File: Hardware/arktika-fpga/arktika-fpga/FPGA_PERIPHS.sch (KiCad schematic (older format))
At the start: 29 parts

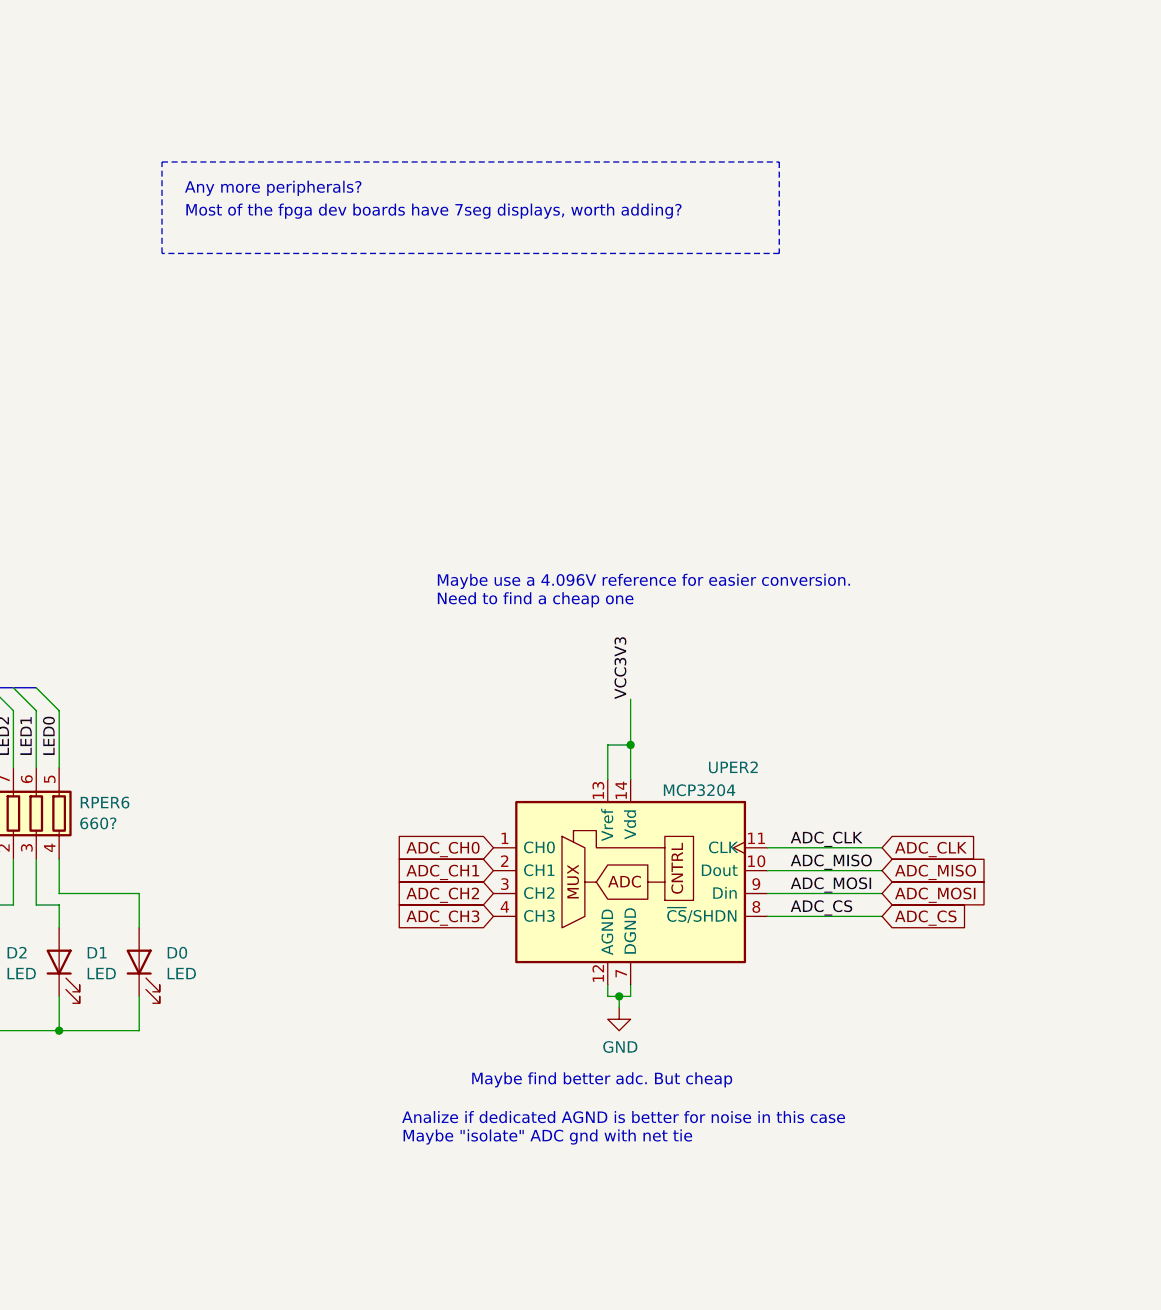
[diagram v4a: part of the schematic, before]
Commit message: Finished routing, did gnd planes, added more silkscreen and some manual via stitching. Pre-final layout.
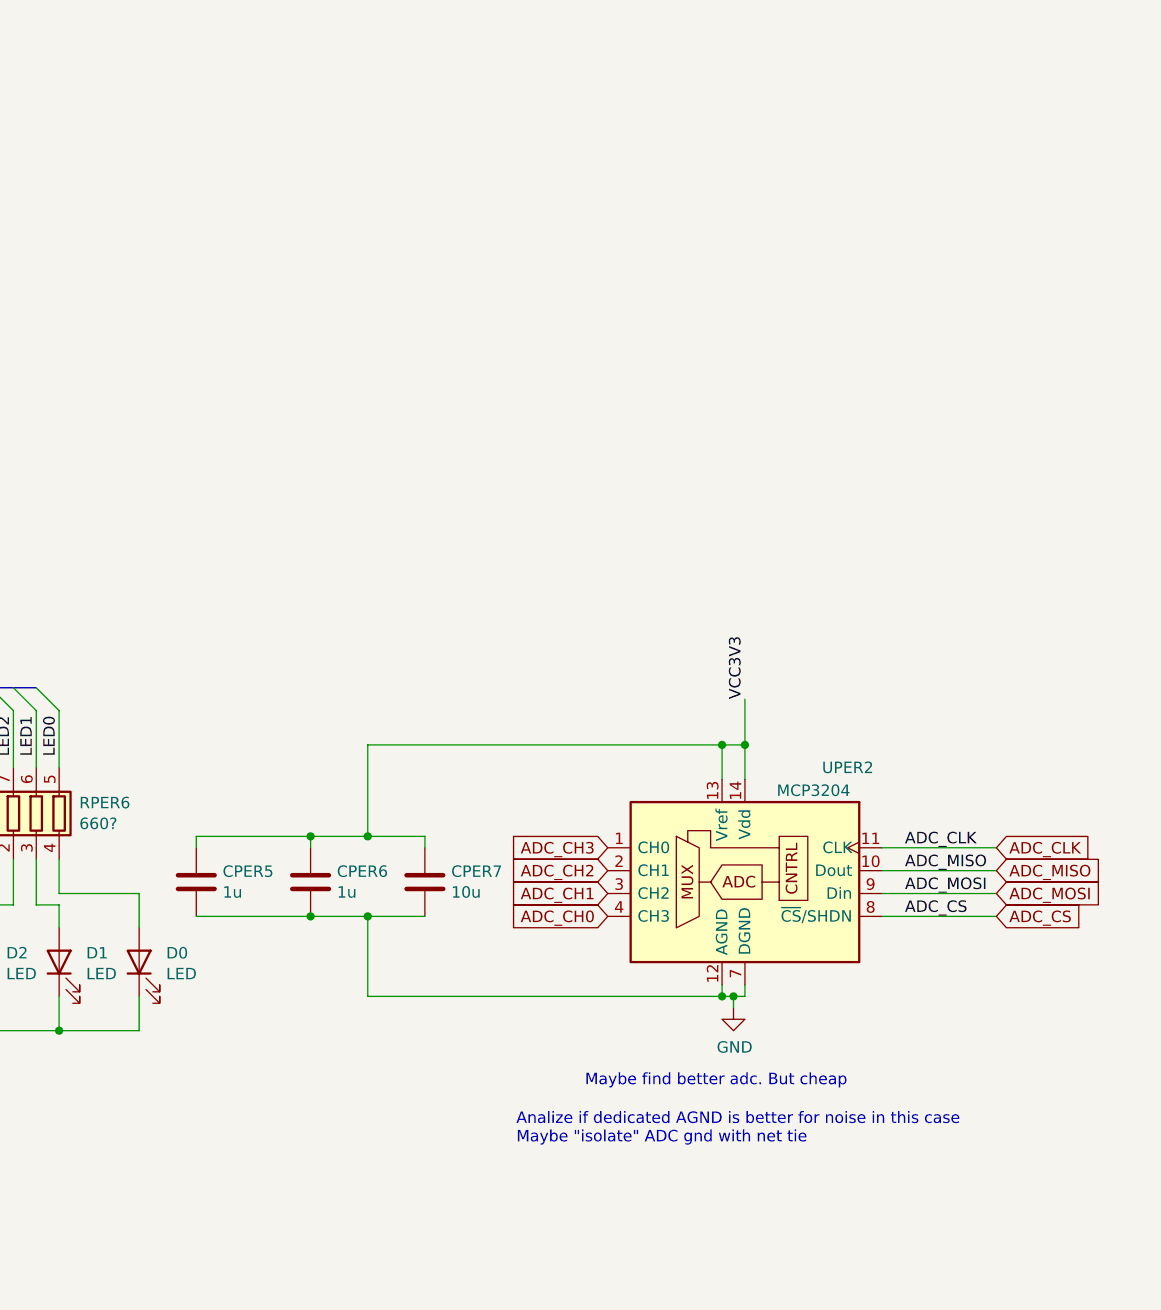
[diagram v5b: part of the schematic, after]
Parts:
- added CPER5, CPER6: 1u, Capacitor_SMD:C_0603_1608Metric_Pad1.05x0.95mm_HandSolder, symbol arktika-fpga-rescue:C-Device
- added CPER7: 10u, Capacitor_SMD:C_0603_1608Metric_Pad1.05x0.95mm_HandSolder, symbol arktika-fpga-rescue:C-Device
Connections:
- net ADC_CH0: now also UPER2.4 (CH3); no longer UPER2.1 (CH0)
- net ADC_CH1: now also UPER2.3 (CH2); no longer UPER2.2 (CH1)
- net ADC_CH2: now also UPER2.2 (CH1); no longer UPER2.3 (CH2)
- net ADC_CH3: now also UPER2.1 (CH0); no longer UPER2.4 (CH3)
- net GND: now also CPER5.2, CPER6.2, CPER7.2
- net VCC3V3: now also CPER5.1, CPER6.1, CPER7.1
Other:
- note removed: "Any more peripherals?"
- note removed: "Maybe use a 4.096V reference for easier conversion.\nNeed to find a cheap one"
- note removed: "Most of the fpga dev boards have 7seg displays, worth adding?"
- moved on the sheet: UPER2
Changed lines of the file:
@@
 L arktika-fpga-rescue:MCP3204-Analog_ADC UPER2
 U 1 1 5F72040D
-P 8950 5000
+P 9450 5000
 AR Path="/5F72040D" Ref="UPER2"  Part="1"
 AR Path="/5F72015E/5F72040D" Ref="UPER2"  Part="1"
-F 0 "UPER2" H 9400 5450 50  0000 C CNN
-F 1 "MCP3204" H 9250 5350 50  0000 C CNN
-F 2 "Package_SO:SOIC-14_3.9x8.7mm_P1.27mm" H 9850 4700 50  0001 C CNN
-F 3 "http://ww1.microchip.com/downloads/en/DeviceDoc/21298c.pdf" H 9850 4700 50  0001 C CNN
-	1    8950 5000
+F 0 "UPER2" H 9900 5450 50  0000 C CNN
+F 1 "MCP3204" H 9750 5350 50  0000 C CNN
+F 2 "Package_SO:SOIC-14_3.9x8.7mm_P1.27mm" H 10350 4700 50  0001 C CNN
+F 3 "http://ww1.microchip.com/downloads/en/DeviceDoc/21298c.pdf" H 10350 4700 50  0001 C CNN
+	1    9450 5000
 	1    0    0    -1
 $EndComp
@@
 	1    0    0    -1
 $EndComp
-Text Label 9650 4900 0    50   ~ 0
+Text Label 10150 4900 0    50   ~ 0
 ADC_CLK
-Text Label 9650 5000 0    50   ~ 0
+Text Label 10150 5000 0    50   ~ 0
 ADC_MISO
-Text Label 9650 5100 0    50   ~ 0
+Text Label 10150 5100 0    50   ~ 0
 ADC_MOSI
-Text Label 9650 5200 0    50   ~ 0
+Text Label 10150 5200 0    50   ~ 0
 ADC_CS
 Wire Wire Line
-	9550 4900 10050 4900
-Wire Wire Line
-	10050 5000 9550 5000
-Wire Wire Line
-	9550 5100 10050 5100
-Wire Wire Line
-	10050 5200 9550 5200
+	10050 4900 10550 4900
+Wire Wire Line
+	10550 5000 10050 5000
+Wire Wire Line
+	10050 5100 10550 5100
+Wire Wire Line
+	10550 5200 10050 5200
 Text HLabel 1250 7200 0    50   Input ~ 0
 SW[0..7]
@@
 Text Label 1800 950  0    50   ~ 0
 VCC3V3
-Text Notes 8250 5950 0    50   ~ 0
+Text Notes 8750 5950 0    50   ~ 0
 Maybe find better adc. But cheap\n
 Text Notes 2850 800  0    50   ~ 0
@@
 L arktika-fpga-rescue:GND-power #PWR0155
 U 1 1 5F6F2DE0
-P 8900 5600
-F 0 "#PWR0155" H 8900 5350 50  0001 C CNN
-F 1 "GND" H 8905 5427 50  0000 C CNN
-F 2 "" H 8900 5600 50  0001 C CNN
-F 3 "" H 8900 5600 50  0001 C CNN
-	1    8900 5600
-	1    0    0    -1
-$EndComp
-Wire Wire Line
-	8850 5500 8850 5550
-Wire Wire Line
-	8850 5550 8900 5550
-Wire Wire Line
-	8950 5550 8950 5500
-Wire Wire Line
-	8900 5550 8900 5600
-Connection ~ 8900 5550
-Wire Wire Line
-	8900 5550 8950 5550
-Text Notes 7950 6200 0    50   ~ 0
+P 9400 5600
+F 0 "#PWR0155" H 9400 5350 50  0001 C CNN
+F 1 "GND" H 9405 5427 50  0000 C CNN
+F 2 "" H 9400 5600 50  0001 C CNN
+F 3 "" H 9400 5600 50  0001 C CNN
+	1    9400 5600
+	1    0    0    -1
+$EndComp
+Wire Wire Line
+	9350 5500 9350 5550
+Wire Wire Line
+	9350 5550 9400 5550
+Wire Wire Line
+	9450 5550 9450 5500
+Wire Wire Line
+	9400 5550 9400 5600
+Connection ~ 9400 5550
+Wire Wire Line
+	9400 5550 9450 5550
+Text Notes 8450 6200 0    50   ~ 0
 Analize if dedicated AGND is better for noise in this case\nMaybe "isolate" ADC gnd with net tie
-Text Label 8950 4250 1    50   ~ 0
+Text Label 9450 4250 1    50   ~ 0
 VCC3V3
 Wire Wire Line
-	8950 4250 8950 4450
-Wire Wire Line
-	8850 4600 8850 4450
-Wire Wire Line
-	8850 4450 8950 4450
-Connection ~ 8950 4450
-Wire Wire Line
-	8950 4450 8950 4600
-Text Notes 8100 3850 0    50   ~ 0
-Maybe use a 4.096V reference for easier conversion.\nNeed to find a cheap one
-Text Notes 7000 2050 0    50   ~ 0
-Any more peripherals?
-Text Notes 7000 2150 0    50   ~ 0
-Most of the fpga dev boards have 7seg displays, worth adding?
-Wire Notes Line
-	6900 1900 9600 1900
-Wire Notes Line
-	9600 1900 9600 2300
-Wire Notes Line
-	9600 2300 6900 2300
-Wire Notes Line
-	6900 2300 6900 1900
+	9450 4250 9450 4450
+Wire Wire Line
+	9350 4600 9350 4450
+Wire Wire Line
+	9350 4450 9450 4450
+Connection ~ 9450 4450
+Wire Wire Line
+	9450 4450 9450 4600
 Connection ~ 2250 1600
 Wire Wire Line
@@
 Text Label 1350 7300 0    50   ~ 0
 LED[0..7]
-Text GLabel 8350 4900 0    50   Input ~ 0
+Text GLabel 8850 5200 0    50   Input ~ 0
 ADC_CH0
-Text GLabel 8350 5000 0    50   Input ~ 0
+Text GLabel 8850 5100 0    50   Input ~ 0
 ADC_CH1
-Text GLabel 8350 5100 0    50   Input ~ 0
+Text GLabel 8850 5000 0    50   Input ~ 0
 ADC_CH2
-Text GLabel 8350 5200 0    50   Input ~ 0
+Text GLabel 8850 4900 0    50   Input ~ 0
 ADC_CH3
-Text GLabel 10050 4900 2    50   Input ~ 0
+Text GLabel 10550 4900 2    50   Input ~ 0
 ADC_CLK
-Text GLabel 10050 5000 2    50   Input ~ 0
+Text GLabel 10550 5000 2    50   Input ~ 0
 ADC_MISO
-Text GLabel 10050 5100 2    50   Input ~ 0
+Text GLabel 10550 5100 2    50   Input ~ 0
 ADC_MOSI
-Text GLabel 10050 5200 2    50   Input ~ 0
+Text GLabel 10550 5200 2    50   Input ~ 0
 ADC_CS
 Text GLabel 4650 1400 2    50   Input ~ 0
@@
 Text GLabel 4650 1500 2    50   Input ~ 0
 UART_TX
-Wire Bus Line
-	2450 4800 3450 4800
-Wire Bus Line
-	650  5150 2000 5150
-Wire Bus Line
-	4550 4200 6350 4200
 Wire Wire Line
 	2900 7150 3300 7150
@@
 	1    0    0    -1
 $EndComp
+$Comp
+L arktika-fpga-rescue:C-Device CPER7
+U 1 1 5FC72ECB
+P 8050 5050
+F 0 "CPER7" H 8165 5096 50  0000 L CNN
+F 1 "10u" H 8165 5005 50  0000 L CNN
+F 2 "Capacitor_SMD:C_0603_1608Metric_Pad1.05x0.95mm_HandSolder" H 8088 4900 50  0001 C CNN
+F 3 "~" H 8050 5050 50  0001 C CNN
+	1    8050 5050
+	1    0    0    -1
+$EndComp
+$Comp
+L arktika-fpga-rescue:C-Device CPER6
+U 1 1 5FC76AE0
+P 7550 5050
+F 0 "CPER6" H 7665 5096 50  0000 L CNN
+F 1 "1u" H 7665 5005 50  0000 L CNN
+F 2 "Capacitor_SMD:C_0603_1608Metric_Pad1.05x0.95mm_HandSolder" H 7588 4900 50  0001 C CNN
+F 3 "~" H 7550 5050 50  0001 C CNN
+	1    7550 5050
+	1    0    0    -1
+$EndComp
+Wire Wire Line
+	7800 4450 7800 4850
+Wire Wire Line
+	7800 4850 7550 4850
+Wire Wire Line
+	7550 4850 7550 4900
+Connection ~ 9350 4450
+Wire Wire Line
+	9350 4450 7800 4450
+Wire Wire Line
+	7800 4850 8050 4850
+Wire Wire Line
+	8050 4850 8050 4900
+Connection ~ 7800 4850
+Wire Wire Line
+	7800 5550 7800 5200
+Connection ~ 9350 5550
+Wire Wire Line
+	9350 5550 7800 5550
+Wire Wire Line
+	7800 5200 8050 5200
+Connection ~ 7800 5200
+$Comp
+L arktika-fpga-rescue:C-Device CPER5
+U 1 1 5FCC1DD9
+P 7050 5050
+F 0 "CPER5" H 7165 5096 50  0000 L CNN
+F 1 "1u" H 7165 5005 50  0000 L CNN
+F 2 "Capacitor_SMD:C_0603_1608Metric_Pad1.05x0.95mm_HandSolder" H 7088 4900 50  0001 C CNN
+F 3 "~" H 7050 5050 50  0001 C CNN
+	1    7050 5050
+	1    0    0    -1
+$EndComp
+Wire Wire Line
+	7050 5200 7550 5200
+Connection ~ 7550 5200
+Wire Wire Line
+	7550 5200 7800 5200
+Wire Wire Line
+	7550 4850 7050 4850
+Wire Wire Line
+	7050 4850 7050 4900
+Connection ~ 7550 4850
+Wire Bus Line
+	650  5150 2000 5150
+Wire Bus Line
+	2450 4800 3450 4800
+Wire Bus Line
+	4550 4200 6350 4200
 $EndSCHEMATC

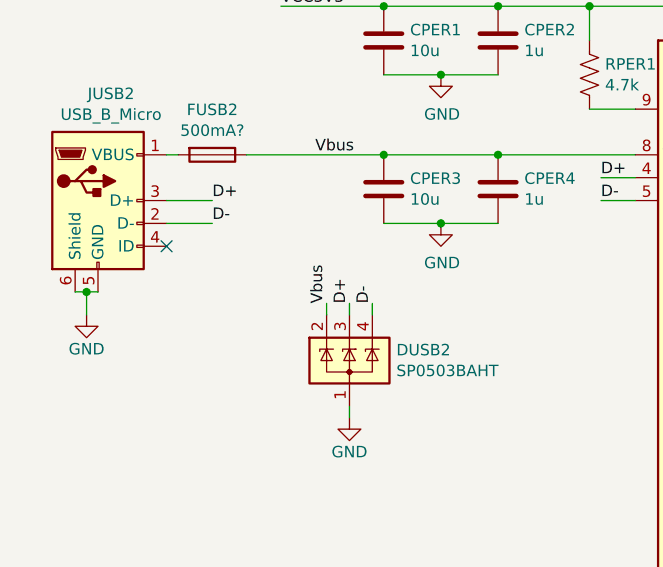
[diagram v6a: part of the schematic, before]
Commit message: Minor layout fixes. Added new micro usb connector footprint and link. Misc silk changes
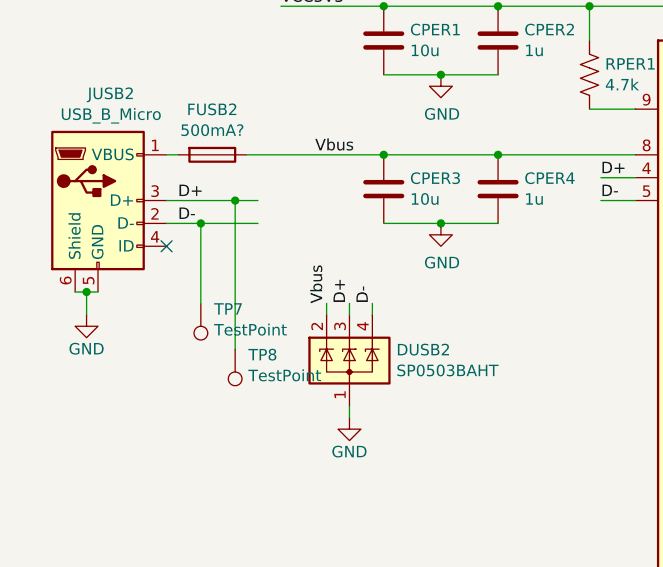
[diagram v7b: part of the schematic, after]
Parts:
- added TP7, TP8: TestPoint, Connector_Pin:Pin_D0.7mm_L6.5mm_W1.8mm_FlatFork, symbol Connector:TestPoint
- JUSB2: footprint Connectors:USB_Micro-B -> Connector_USB:USB_Micro-B_Molex-105017-0001
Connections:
- net D+: now also TP8.1
- net D-: now also TP7.1
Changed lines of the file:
@@
 	1    0    0    -1
 $EndComp
-Text Label 1500 1900 0    50   ~ 0
+Text Label 1350 1900 0    50   ~ 0
 D-
-Text Label 1500 1800 0    50   ~ 0
+Text Label 1350 1800 0    50   ~ 0
 D+
 Text Label 1950 1600 0    50   ~ 0
@@
 F 0 "JUSB2" H 1057 2267 50  0000 C CNN
 F 1 "USB_B_Micro" H 1057 2176 50  0000 C CNN
-F 2 "Connectors:USB_Micro-B" H 1150 1750 50  0001 C CNN
+F 2 "Connector_USB:USB_Micro-B_Molex-105017-0001" H 1150 1750 50  0001 C CNN
 F 3 "~" H 1150 1750 50  0001 C CNN
 	1    1000 1800
@@
 $EndComp
 Wire Wire Line
-	1500 1800 1300 1800
-Wire Wire Line
-	1300 1900 1500 1900
+	1300 1900 1450 1900
 Wire Wire Line
 	2750 950  3150 950
@@
 	7050 4850 7050 4900
 Connection ~ 7550 4850
+$Comp
+L Connector:TestPoint TP?
+U 1 1 5F32DF20
+P 1450 2250
+AR Path="/5F3E98C5/5F32DF20" Ref="TP?"  Part="1"
+AR Path="/5F72015E/5F32DF20" Ref="TP7"  Part="1"
+F 0 "TP7" H 1392 2276 50  0000 R CNN
+F 1 "TestPoint" H 1392 2367 50  0000 R CNN
+F 2 "Connector_Pin:Pin_D0.7mm_L6.5mm_W1.8mm_FlatFork" H 1650 2250 50  0001 C CNN
+F 3 "~" H 1650 2250 50  0001 C CNN
+	1    1450 2250
+	-1   0    0    1
+$EndComp
+$Comp
+L Connector:TestPoint TP?
+U 1 1 5F33AC74
+P 1600 2450
+AR Path="/5F3E98C5/5F33AC74" Ref="TP?"  Part="1"
+AR Path="/5F72015E/5F33AC74" Ref="TP8"  Part="1"
+F 0 "TP8" H 1542 2476 50  0000 R CNN
+F 1 "TestPoint" H 1542 2567 50  0000 R CNN
+F 2 "Connector_Pin:Pin_D0.7mm_L6.5mm_W1.8mm_FlatFork" H 1800 2450 50  0001 C CNN
+F 3 "~" H 1800 2450 50  0001 C CNN
+	1    1600 2450
+	-1   0    0    1
+$EndComp
+Wire Wire Line
+	1450 2250 1450 1900
+Connection ~ 1450 1900
+Wire Wire Line
+	1600 1800 1600 2450
+Wire Wire Line
+	1300 1800 1600 1800
+Wire Wire Line
+	1600 1800 1700 1800
+Connection ~ 1600 1800
+Wire Wire Line
+	1450 1900 1700 1900
 Wire Bus Line
 	650  5150 2000 5150
